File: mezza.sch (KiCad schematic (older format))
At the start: 26 parts, among them CON1 USB-MINI-B, P1 CONN_02X20, P2 CONN_02X20, U2 FT230XS, U3 XC6206

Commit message: Power FTDI Independently, Make File Paths Relative, Add Reg. Footprint
Previously the FTDI was powered by the baseboard. This means it would only
be powered up once the baseboard is on - resulting in a few seconds of data
loss. This has been fixed by providing a different power source for the FTDI.

The mezza library path is now a relative path so it should work on other
computers when cloned.

A footprint for the regulator has been added.

Signed-off-by: Sophie Haynes <sophie.haynes@linaro.org>
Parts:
- removed C1, C2: 1uF, Capacitors_SMD:C_0805, symbol CP
- removed U3: XC6206, mezza:SOT223, symbol AP1117D33
- added C?: CP, symbol CP
- added U?: XC6206_SOT23, mezza:SOT-23_Seeed, symbol XC6206_SOT23
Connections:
- net labels added: +1V8_F
- wire segments 155 -> 169
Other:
- moved on the sheet: C6, C7
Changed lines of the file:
@@
 $EndDescr
-$Comp
-L AP1117D33 U3
-U 1 1 55BEAC34
-P 1200 3550
-F 0 "U3" H 1300 3300 50  0000 C CNN
-F 1 "XC6206" H 1200 3800 50  0000 C CNN
-F 2 "mezza:SOT223" H 1200 3550 60  0001 C CNN
-F 3 "" H 1200 3550 60  0000 C CNN
-F 4 "310030097" H -4500 3250 60  0001 C CNN "Seeed SKU"
-F 5 "Jiangsu Changjiang" H -4500 3250 60  0001 C CNN "Mfr"
-F 6 "CJT1117-3.3" H -4500 3250 60  0001 C CNN "Mfr Part #"
-	1    1200 3550
-	1    0    0    -1
-$EndComp
-$Comp
-L GND #PWR01
-U 1 1 55BEB06A
-P 1200 3950
-F 0 "#PWR01" H 1200 3700 50  0001 C CNN
-F 1 "GND" H 1200 3800 50  0000 C CNN
-F 2 "" H 1200 3950 60  0000 C CNN
-F 3 "" H 1200 3950 60  0000 C CNN
-	1    1200 3950
-	1    0    0    -1
-$EndComp
-$Comp
-L CP C2
-U 1 1 55BEB167
-P 1600 3800
-F 0 "C2" H 1625 3900 50  0000 L CNN
-F 1 "1uF" H 1625 3700 50  0000 L CNN
-F 2 "Capacitors_SMD:C_0805" H 1638 3650 30  0001 C CNN
-F 3 "" H 1600 3800 60  0000 C CNN
-F 4 "302010148" H -4500 3250 60  0001 C CNN "Seeed SKU"
-F 5 "Yageo" H -4500 3250 60  0001 C CNN "Mfr"
-F 6 "CC0805KKX7R8BB225" H -4500 3250 60  0001 C CNN "Mfr Part #"
-	1    1600 3800
-	1    0    0    -1
-$EndComp
-$Comp
-L CP C1
-U 1 1 55C57889
-P 750 3800
-F 0 "C1" H 775 3900 50  0000 L CNN
-F 1 "1uF" H 775 3700 50  0000 L CNN
-F 2 "Capacitors_SMD:C_0805" H 788 3650 30  0001 C CNN
-F 3 "" H 750 3800 60  0000 C CNN
-F 4 "302010148" H -4500 3250 60  0001 C CNN "Seeed SKU"
-F 5 "Yageo" H -4500 3250 60  0001 C CNN "Mfr"
-F 6 "CC0805KKX7R8BB225" H -4500 3250 60  0001 C CNN "Mfr Part #"
-	1    750  3800
-	1    0    0    -1
-$EndComp
 $Comp
 L GND #PWR02
@@
 F 3 "" H 3000 2550 60  0000 C CNN
 	1    3000 2550
-	1    0    0    -1
-$EndComp
-$Comp
-L +1V8 #PWR014
-U 1 1 55D44684
-P 1600 3300
-F 0 "#PWR014" H 1600 3150 50  0001 C CNN
-F 1 "+1V8" H 1600 3440 50  0000 C CNN
-F 2 "" H 1600 3300 60  0000 C CNN
-F 3 "" H 1600 3300 60  0000 C CNN
-	1    1600 3300
 	1    0    0    -1
 $EndComp
@@
 	1    0    0    -1
 $EndComp
-$Comp
-L +1V8 #PWR016
-U 1 1 56432A36
-P 3150 4450
-F 0 "#PWR016" H 3150 4300 50  0001 C CNN
-F 1 "+1V8" H 3150 4590 50  0000 C CNN
-F 2 "" H 3150 4450 60  0000 C CNN
-F 3 "" H 3150 4450 60  0000 C CNN
-	1    3150 4450
-	1    0    0    -1
-$EndComp
 Text GLabel 3700 1200 0    60   Input ~ 0
 UART_RX
@@
 L VBUS #PWR022
 U 1 1 564CECA3
-P 2400 3300
-F 0 "#PWR022" H 2400 3400 30  0001 C CNN
-F 1 "VBUS" H 2400 3410 30  0000 C CNN
-F 2 "" H 2400 3300 60  0000 C CNN
-F 3 "" H 2400 3300 60  0000 C CNN
-	1    2400 3300
+P 2500 3300
+F 0 "#PWR022" H 2500 3400 30  0001 C CNN
+F 1 "VBUS" H 2500 3410 30  0000 C CNN
+F 2 "" H 2500 3300 60  0000 C CNN
+F 3 "" H 2500 3300 60  0000 C CNN
+	1    2500 3300
 	1    0    0    -1
 $EndComp
@@
 L C_Small C6
 U 1 1 564CED04
-P 2150 3650
-F 0 "C6" H 2160 3720 50  0000 L CNN
-F 1 "1uF" H 2160 3570 50  0000 L CNN
-F 2 "Capacitors_SMD:C_0603" H 2150 3650 60  0001 C CNN
-F 3 "" H 2150 3650 60  0000 C CNN
-	1    2150 3650
+P 2250 3650
+F 0 "C6" H 2260 3720 50  0000 L CNN
+F 1 "1uF" H 2260 3570 50  0000 L CNN
+F 2 "Capacitors_SMD:C_0603" H 2250 3650 60  0001 C CNN
+F 3 "" H 2250 3650 60  0000 C CNN
+	1    2250 3650
 	1    0    0    -1
 $EndComp
@@
 L C_Small C7
 U 1 1 564CED40
-P 2650 3650
-F 0 "C7" H 2660 3720 50  0000 L CNN
-F 1 "100nF" H 2660 3570 50  0000 L CNN
-F 2 "Capacitors_SMD:C_0603" H 2650 3650 60  0001 C CNN
-F 3 "" H 2650 3650 60  0000 C CNN
-	1    2650 3650
+P 2750 3650
+F 0 "C7" H 2760 3720 50  0000 L CNN
+F 1 "100nF" H 2760 3570 50  0000 L CNN
+F 2 "Capacitors_SMD:C_0603" H 2750 3650 60  0001 C CNN
+F 3 "" H 2750 3650 60  0000 C CNN
+	1    2750 3650
 	1    0    0    -1
 $EndComp
@@
 L GND #PWR023
 U 1 1 564CEDC1
-P 2400 3950
-F 0 "#PWR023" H 2400 3700 50  0001 C CNN
-F 1 "GND" H 2400 3800 50  0000 C CNN
-F 2 "" H 2400 3950 60  0000 C CNN
-F 3 "" H 2400 3950 60  0000 C CNN
-	1    2400 3950
+P 2500 3950
+F 0 "#PWR023" H 2500 3700 50  0001 C CNN
+F 1 "GND" H 2500 3800 50  0000 C CNN
+F 2 "" H 2500 3950 60  0000 C CNN
+F 3 "" H 2500 3950 60  0000 C CNN
+	1    2500 3950
 	1    0    0    -1
 $EndComp
@@
 $EndComp
 Wire Wire Line
-	1850 5250 2400 5250
+	1850 5250 2000 5250
+Wire Wire Line
+	2000 5250 2150 5250
+Wire Wire Line
+	2150 5250 2400 5250
 Wire Wire Line
 	1900 4650 1850 4650
@@
 	4350 1000 4450 1000
 Wire Wire Line
-	2150 3850 2650 3850
-Wire Wire Line
-	2650 3850 2650 3750
-Wire Wire Line
-	2150 3450 2650 3450
-Wire Wire Line
-	2650 3450 2650 3550
-Connection ~ 2400 3850
-Wire Wire Line
-	2400 3850 2400 3950
-Wire Wire Line
-	2150 3750 2150 3850
-Connection ~ 2400 3450
-Wire Wire Line
-	2150 3450 2150 3550
-Wire Wire Line
-	2400 3300 2400 3450
+	2250 3850 2500 3850
+Wire Wire Line
+	2500 3850 2750 3850
+Wire Wire Line
+	2750 3850 2750 3750
+Wire Wire Line
+	2250 3450 2500 3450
+Wire Wire Line
+	2500 3450 2750 3450
+Wire Wire Line
+	2750 3450 2750 3550
+Connection ~ 2500 3850
+Wire Wire Line
+	2500 3850 2500 3950
+Wire Wire Line
+	2250 3750 2250 3850
+Connection ~ 2500 3450
+Wire Wire Line
+	2250 3450 2250 3550
+Wire Wire Line
+	2500 3300 2500 3450
 Wire Wire Line
 	2950 4550 3350 4550
@@
 Connection ~ 750  5250
 Wire Wire Line
-	750  4650 750  5350
+	750  4650 750  4800
+Wire Wire Line
+	750  4800 750  5100
+Wire Wire Line
+	750  5100 750  5250
+Wire Wire Line
+	750  5250 750  5350
 Connection ~ 3150 5200
 Wire Wire Line
 	3350 5200 3150 5200
 Wire Wire Line
-	3150 5100 3150 5850
+	3150 5100 3150 5200
+Wire Wire Line
+	3150 5200 3150 5700
+Wire Wire Line
+	3150 5700 3150 5850
 Wire Wire Line
 	5200 5500 5750 5500
@@
 	4300 6450 4300 6400
 Wire Wire Line
-	4150 6400 4450 6400
+	4150 6400 4300 6400
+Wire Wire Line
+	4300 6400 4450 6400
 Wire Wire Line
 	5350 4600 5200 4600
@@
 	4350 2600 4400 2600
 Wire Wire Line
-	4350 2700 4450 2700
+	4350 2700 4400 2700
+Wire Wire Line
+	4400 2700 4450 2700
 Wire Wire Line
 	3700 700  3700 750
@@
 Wire Wire Line
 	2300 700  2300 750
-Wire Wire Line
-	1500 3550 1600 3550
 Wire Wire Line
 	800  2550 800  2700
@@
 	2150 2600 2200 2600
 Wire Wire Line
-	2150 2700 2250 2700
+	2150 2700 2200 2700
+Wire Wire Line
+	2200 2700 2250 2700
 Wire Wire Line
 	1500 700  1500 750
@@
 Wire Wire Line
 	1650 1300 1500 1300
-Wire Wire Line
-	750  3550 900  3550
-Wire Wire Line
-	1200 3850 1200 3950
-Connection ~ 750  3550
-Wire Wire Line
-	750  3300 750  3650
-Connection ~ 1200 3950
-Connection ~ 1600 3550
-Wire Wire Line
-	1600 3300 1600 3650
-Wire Wire Line
-	750  3950 1600 3950
 Connection ~ 2000 5250
 Connection ~ 2150 5250
 Wire Wire Line
-	1850 4800 2600 4800
-Wire Wire Line
-	1950 4900 2600 4900
+	1850 4800 2400 4800
+Wire Wire Line
+	2400 4800 2600 4800
+Wire Wire Line
+	1950 4900 2150 4900
+Wire Wire Line
+	2150 4900 2600 4900
 Wire Wire Line
 	1950 4900 1950 4950
@@
 	1100 6400 1100 6650
 Wire Wire Line
-	750  5950 1100 5950
+	750  5950 950  5950
+Wire Wire Line
+	950  5950 1100 5950
 Wire Wire Line
 	1100 5950 1100 6100
@@
 GPIO_L
 $Comp
+L XC6206_SOT23 U?
+U 1 1 567C90F0
+P 1250 3700
+F 0 "U?" H 1250 4000 60  0000 C CNN
+F 1 "XC6206_SOT23" H 1300 3450 60  0000 L CNN
+F 2 "mezza:SOT-23_Seeed" H 1250 3700 60  0001 C CNN
+F 3 "" H 1250 3700 60  0000 C CNN
+F 4 "310030016" H 1250 3700 60  0001 C CNN "Seeed SKU"
+F 5 "Torex" H 1250 3700 60  0001 C CNN "manf"
+F 6 "XC6206P182MR" H 1250 3700 60  0001 C CNN "manf#"
+	1    1250 3700
+	1    0    0    -1
+$EndComp
+$Comp
 L +3V3_F #PWR?
-U 1 1 56685B3D
-P 750 3300
-F 0 "#PWR?" H 750 3150 50  0001 C CNN
-F 1 "+3V3_F" H 750 3440 50  0000 C CNN
-F 2 "" H 750 3300 60  0000 C CNN
-F 3 "" H 750 3300 60  0000 C CNN
-	1    750  3300
-	1    0    0    -1
-$EndComp
+U 1 1 567C95A5
+P 700 3550
+F 0 "#PWR?" H 700 3400 50  0001 C CNN
+F 1 "+3V3_F" H 700 3690 50  0000 C CNN
+F 2 "" H 700 3550 60  0000 C CNN
+F 3 "" H 700 3550 60  0000 C CNN
+	1    700  3550
+	1    0    0    -1
+$EndComp
+Wire Wire Line
+	700  3550 900  3550
+$Comp
+L GND #PWR?
+U 1 1 567C96FE
+P 1250 3900
+F 0 "#PWR?" H 1250 3650 50  0001 C CNN
+F 1 "GND" H 1250 3750 50  0000 C CNN
+F 2 "" H 1250 3900 60  0000 C CNN
+F 3 "" H 1250 3900 60  0000 C CNN
+	1    1250 3900
+	1    0    0    -1
+$EndComp
+Wire Wire Line
+	1850 3550 1650 3550
+Wire Wire Line
+	1650 3550 1600 3550
+$Comp
+L CP C?
+U 1 1 567CA0AC
+P 1650 3750
+F 0 "C?" H 1675 3850 50  0000 L CNN
+F 1 "CP" H 1675 3650 50  0000 L CNN
+F 2 "" H 1688 3600 30  0000 C CNN
+F 3 "" H 1650 3750 60  0000 C CNN
+	1    1650 3750
+	1    0    0    -1
+$EndComp
+Wire Wire Line
+	1650 3600 1650 3550
+Connection ~ 1650 3550
+Wire Wire Line
+	1650 3900 1250 3900
+$Comp
+L +1V8_F #PWR?
+U 1 1 567CA860
+P 1850 3550
+F 0 "#PWR?" H 1850 3400 50  0001 C CNN
+F 1 "+1V8_F" H 1850 3690 50  0000 C CNN
+F 2 "" H 1850 3550 60  0000 C CNN
+F 3 "" H 1850 3550 60  0000 C CNN
+	1    1850 3550
+	1    0    0    -1
+$EndComp
+$Comp
+L +1V8_F #PWR?
+U 1 1 567CABFC
+P 3150 4450
+F 0 "#PWR?" H 3150 4300 50  0001 C CNN
+F 1 "+1V8_F" H 3150 4590 50  0000 C CNN
+F 2 "" H 3150 4450 60  0000 C CNN
+F 3 "" H 3150 4450 60  0000 C CNN
+	1    3150 4450
+	1    0    0    -1
+$EndComp

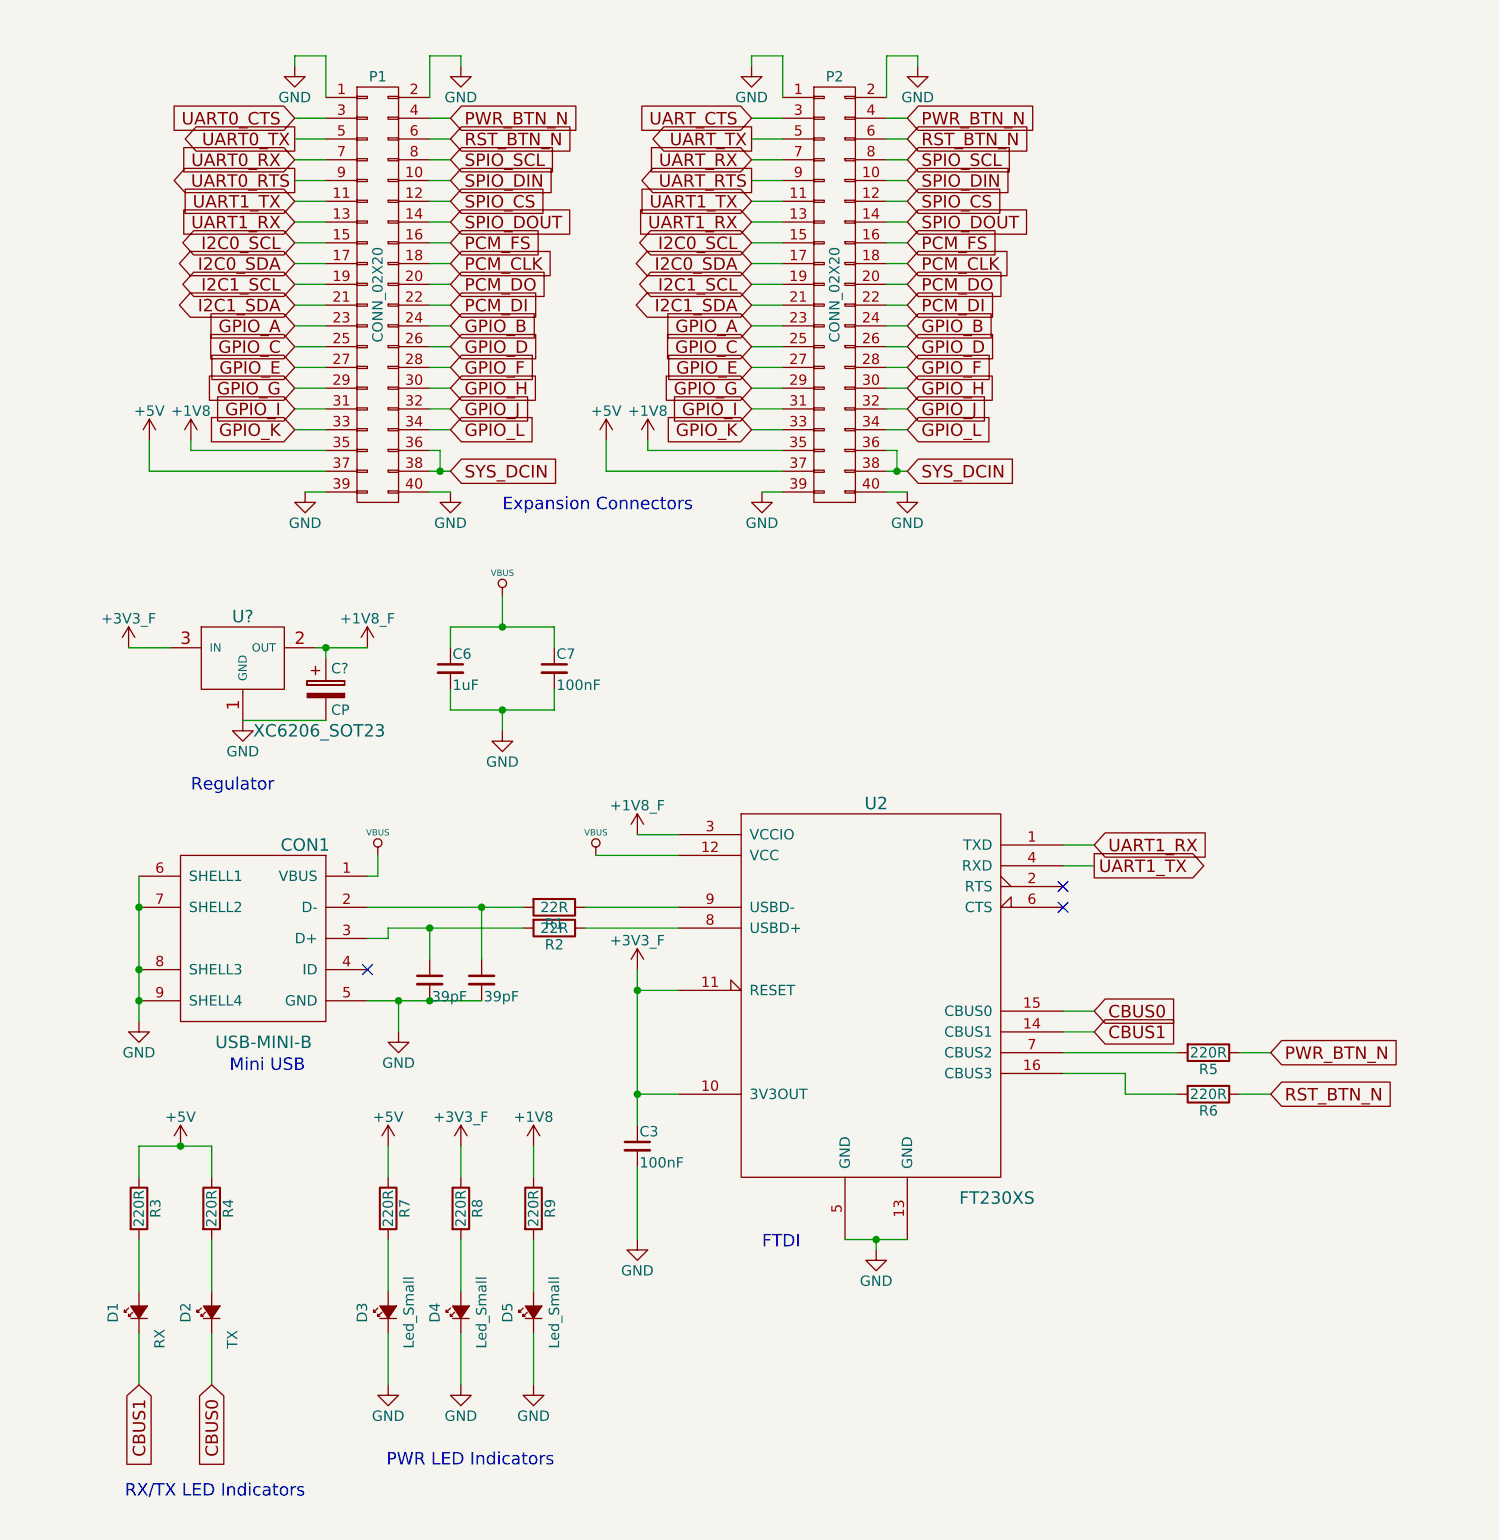
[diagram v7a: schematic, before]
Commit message: Add PWR LED for 1V8_F
Added a LED for the 1V8_F power rail to indicate it's powered on.

Signed-off-by: Sophie Haynes <sophie.haynes@linaro.org>
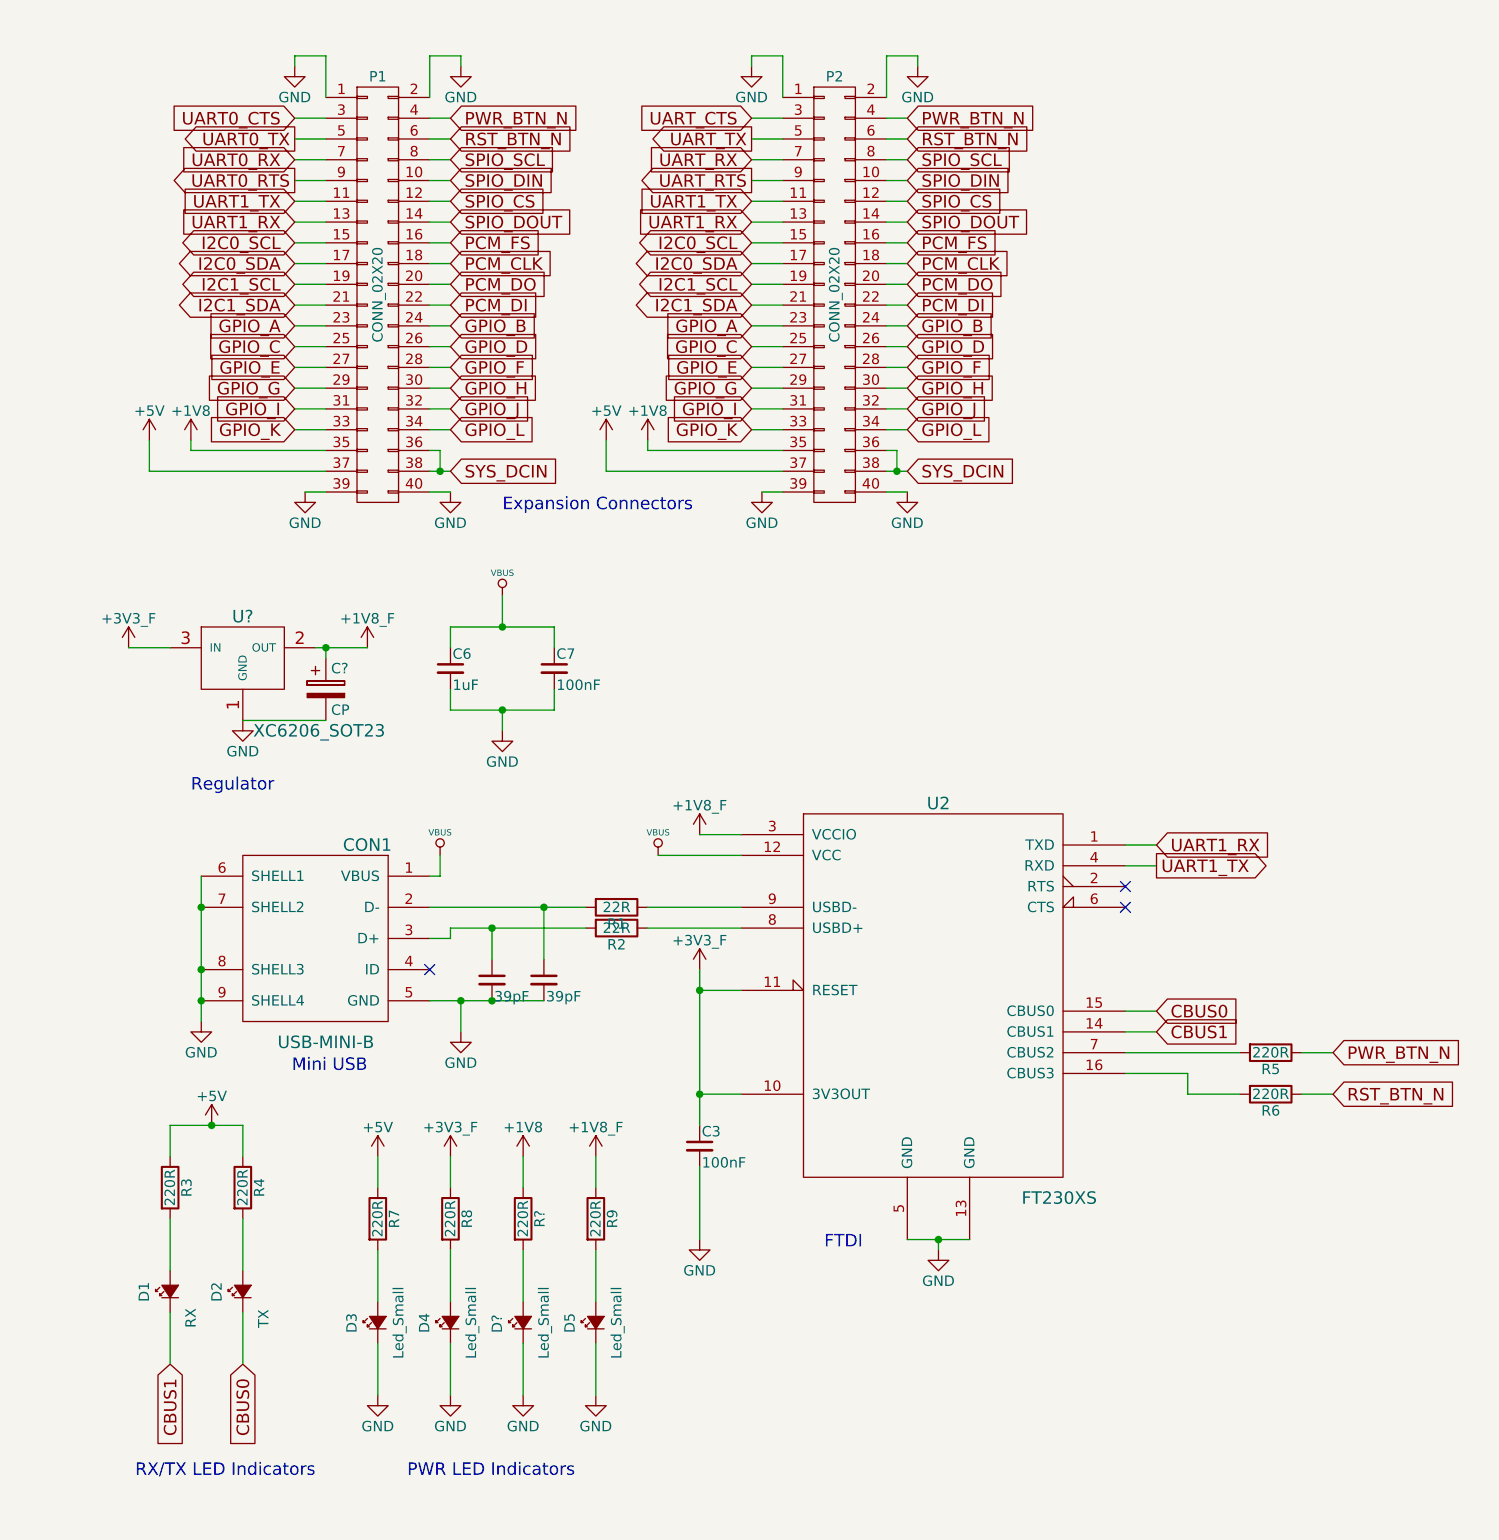
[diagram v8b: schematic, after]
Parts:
- added D?: Led_Small, symbol Led_Small
- added R?: 220R, symbol R
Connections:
- net +1V8: now also R?.1; no longer R9.1
- net +1V8_F: now also R9.1
- net GND: now also D?.1 (K)
- new net: D?.2 (A), R?.2
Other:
- moved on the sheet: C3, CON1, D1, D2, D3, D4, D5, R1, R2, R3, R4, R5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
